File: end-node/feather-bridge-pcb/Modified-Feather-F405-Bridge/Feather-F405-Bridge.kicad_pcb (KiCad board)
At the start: 2 copper layers, 38.7 x 52.3 mm, 16 parts, among them J1 Conn_01x06, J2 Conn_01x06, J3 Conn_02x06_Odd_Even, SW1 SW_SPST, SW2 SW_SPST, U1 LoRa Radio FeatherWing, U2 NUD3112LT1, U3 NUD3112LT1

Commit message: cleanup schematic
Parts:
- U2, U3: footprint Footprints:SOT-23_ONS -> Footprints:SOT-23
- turned U2 to 0 degrees
- turned U3 to 0 degrees
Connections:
- net Net-(J1-Pin_2) renamed REMOTE_DFU
- net Net-(J1-Pin_6) renamed REMOTE_RST

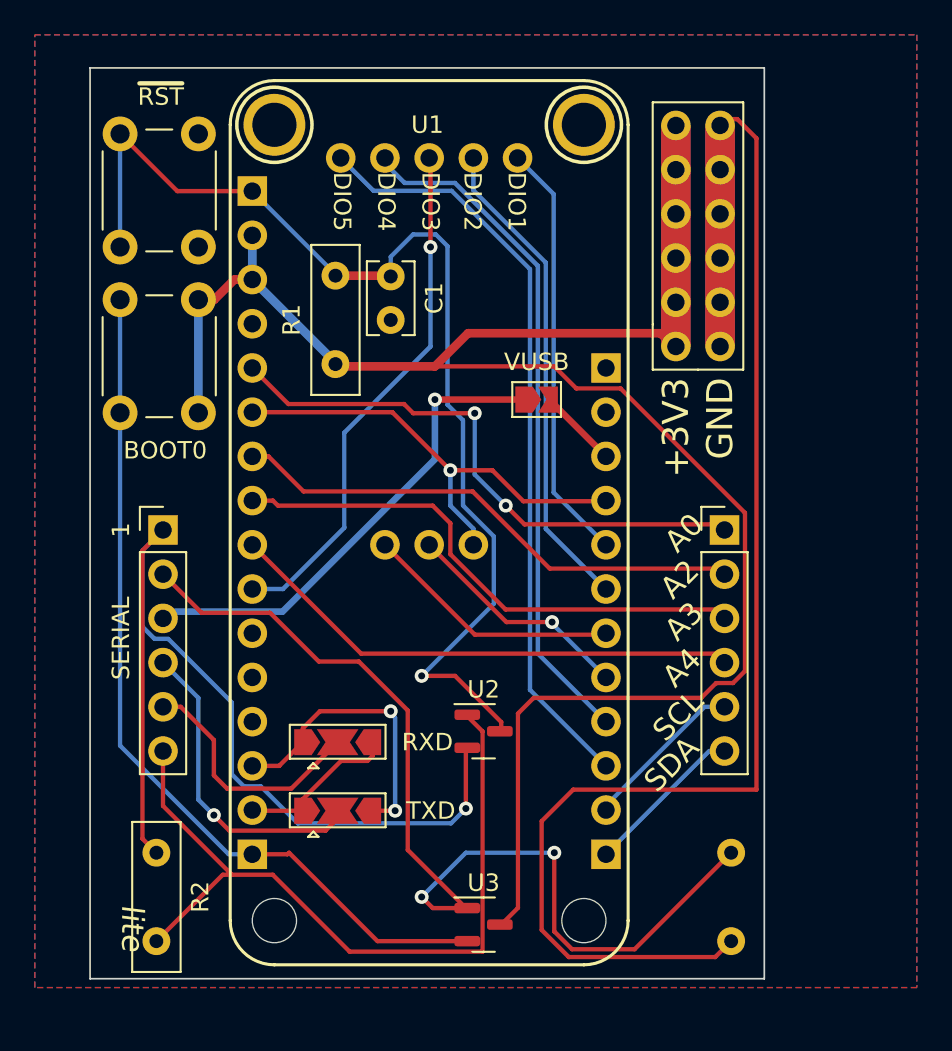
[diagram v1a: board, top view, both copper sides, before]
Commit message: Remove UART RX/TX crossover SB, fix resistor footprints, add separate header for remote dfu/rst, fancy logo
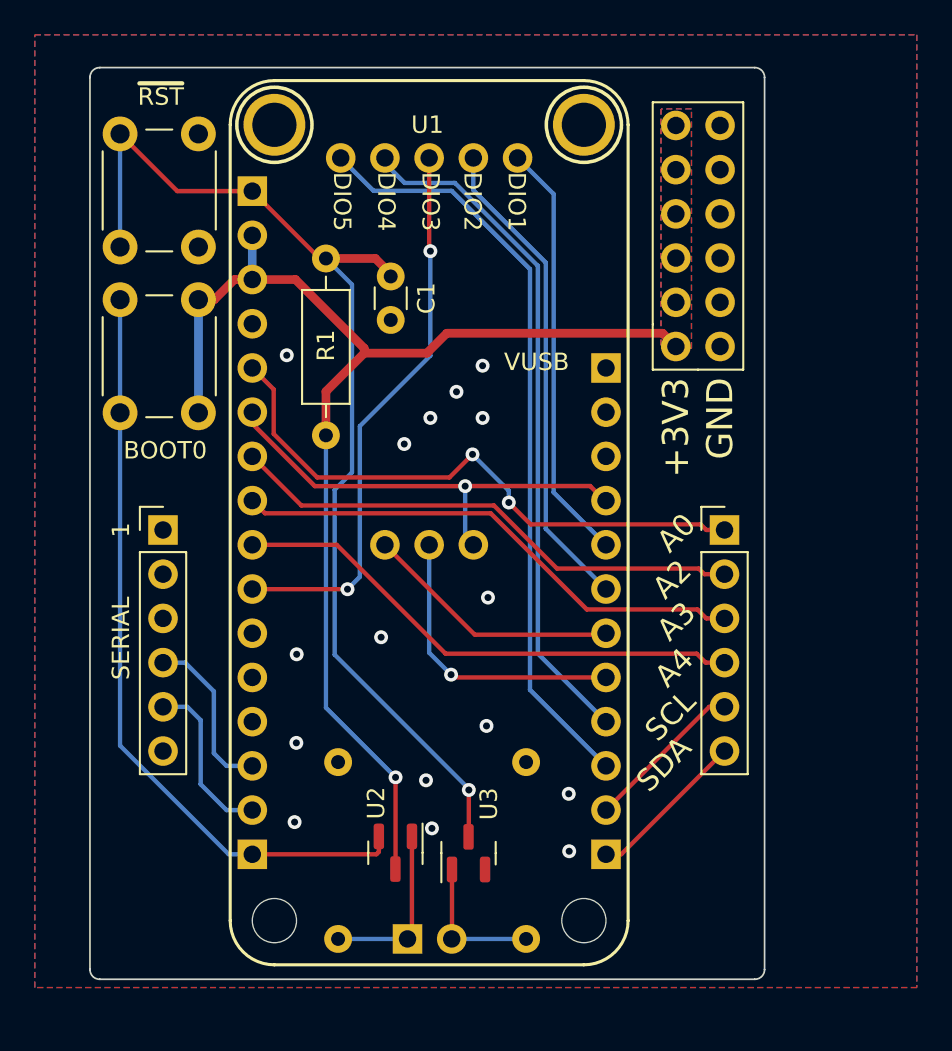
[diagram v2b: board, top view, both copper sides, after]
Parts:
- removed JP1: SolderJumper_2_Open, Footprints:SolderJumper-2_P1.3mm_Open_TrianglePad1.0x1.5mm
- removed JP2, JP3: SolderJumper_3_Open, Footprints:SolderJumper-3_P2.0mm_Open_TrianglePad1.0x1.5mm
- removed the REF** at (47.9, 167.8)
- added J4: Conn_01x02, Footprints:PinHeader_1x02_P2.54mm_Horizontal, B.Cu at (62.7, 167.5)
- added REF**: FOAM-Logo-Cubes, Footprints:FOAM-Logo-Cubes, F.Cu at (48.8, 161.3)
- C1: footprint Footprints:C_Rect_L4.0mm_W2.5mm_P2.50mm -> Footprints:C_Disc_D3.0mm_W1.6mm_P2.50mm
- R1, R3: footprint Footprints:R_Box_L8.4mm_W2.5mm_P5.08mm -> Footprints:R_Axial_DIN0207_L6.3mm_D2.5mm_P10.16mm_Horizontal
- R2: footprint Footprints:R_Box_L8.4mm_W2.5mm_P5.08mm -> Footprints:R_Axial_DIN0207_L6.3mm_D2.5mm_P10.16mm_Horizontal; moved to B.Cu
- moved R3 23.1 mm to (58.7, 167.5), turned to 90 degrees
- moved R2 21.9 mm to (69.5, 157.4)
- moved U2 7.06 mm to (66.2, 162.6), turned to 90 degrees
- moved U3 6.54 mm to (62.0, 162.6), turned to -90 degrees
- moved R1 4.13 mm to (58.0, 138.6)
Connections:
- J1 pad 2: REMOTE_DFU -> unconnected-(J1-Pin_2-Pad2)
- J1 pad 3: Net-(J1-Pin_3) -> unconnected-(J1-Pin_3-Pad3)
- J1 pad 4: /FT232_TXD -> FEATHER_UART_RX
- J1 pad 5: /FT232_RXD -> FEATHER_UART_TX
- J1 pad 6: REMOTE_RST -> unconnected-(J1-Pin_6-Pad6)
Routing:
- net GND: track 126.1 -> 0.00 mm, vias 1 -> 16
- net REMOTE_DFU: track 58.9 -> 9.98 mm, vias 2 -> 0
- net REMOTE_RST: track 44.9 -> 8.27 mm
- net 3V3: track 100.1 -> 71.9 mm, vias 0 -> 1
- net Net-(J1-Pin_3): track 27.4 -> 0.00 mm, vias 1 -> 0
- net /FT232_TXD: track 17.7 -> 0.00 mm, vias 1 -> 0
- net /FT232_RXD: track 14.3 -> 0.00 mm
- net FEATHER_UART_RX: track 16.8 -> 9.67 mm, vias 2 -> 0
- net FEATHER_BOOT0: track 50.2 -> 44.0 mm
- net VUSB: track 4.56 -> 0.00 mm
- net RFM_~{CS}: track 13.4 -> 16.9 mm
- net RFM_DIO3: track 30.0 -> 32.2 mm, vias 1 -> 2
- net FEATHER_A0: track 32.6 -> 34.0 mm
- net FEATHER_~{RST}: track 64.3 -> 62.9 mm
- net FEATHER_A3: track 31.0 -> 29.9 mm
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- added copper zone on B.Cu, net 3V3
- added copper zone on F.Cu, net 3V3
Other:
- board size 38.7 x 52.3 mm -> 38.8 x 52.4 mm
- board text added: "REMOTE_DFU"
- board text added: "REMOTE_RST"
- board text added: "locked"
- board text removed: "RXD"
- board text removed: "TXD"

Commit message: tweak some lines for future changes with BLE
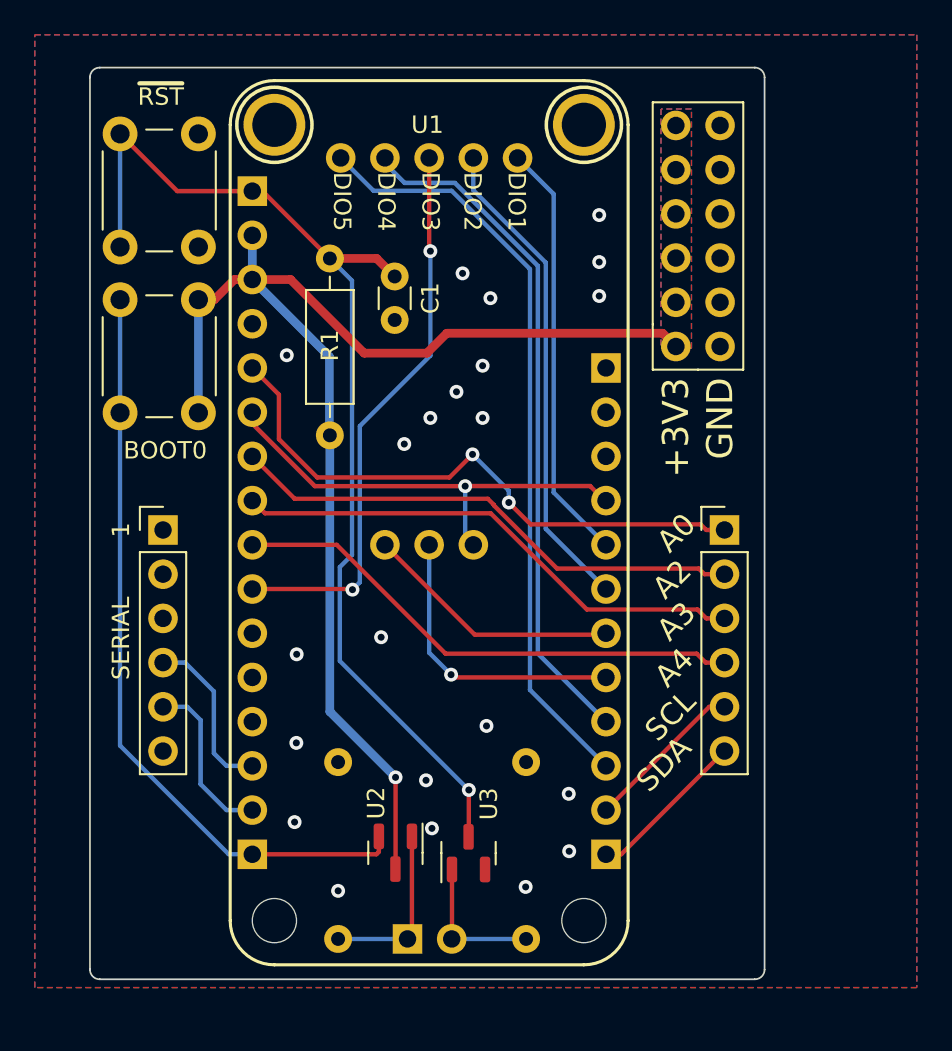
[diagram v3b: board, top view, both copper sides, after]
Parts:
- moved C1 0.23 mm to (62.0, 129.5)
- moved R1 0.23 mm to (58.2, 138.6)
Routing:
- net 3V3: track 71.9 -> 76.8 mm
- net GND: vias 16 -> 22
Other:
- board text removed: "VUSB"
